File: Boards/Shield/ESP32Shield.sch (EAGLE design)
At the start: 30 parts, among them Q1 220mA/50V/3.5Ω, U1 5V

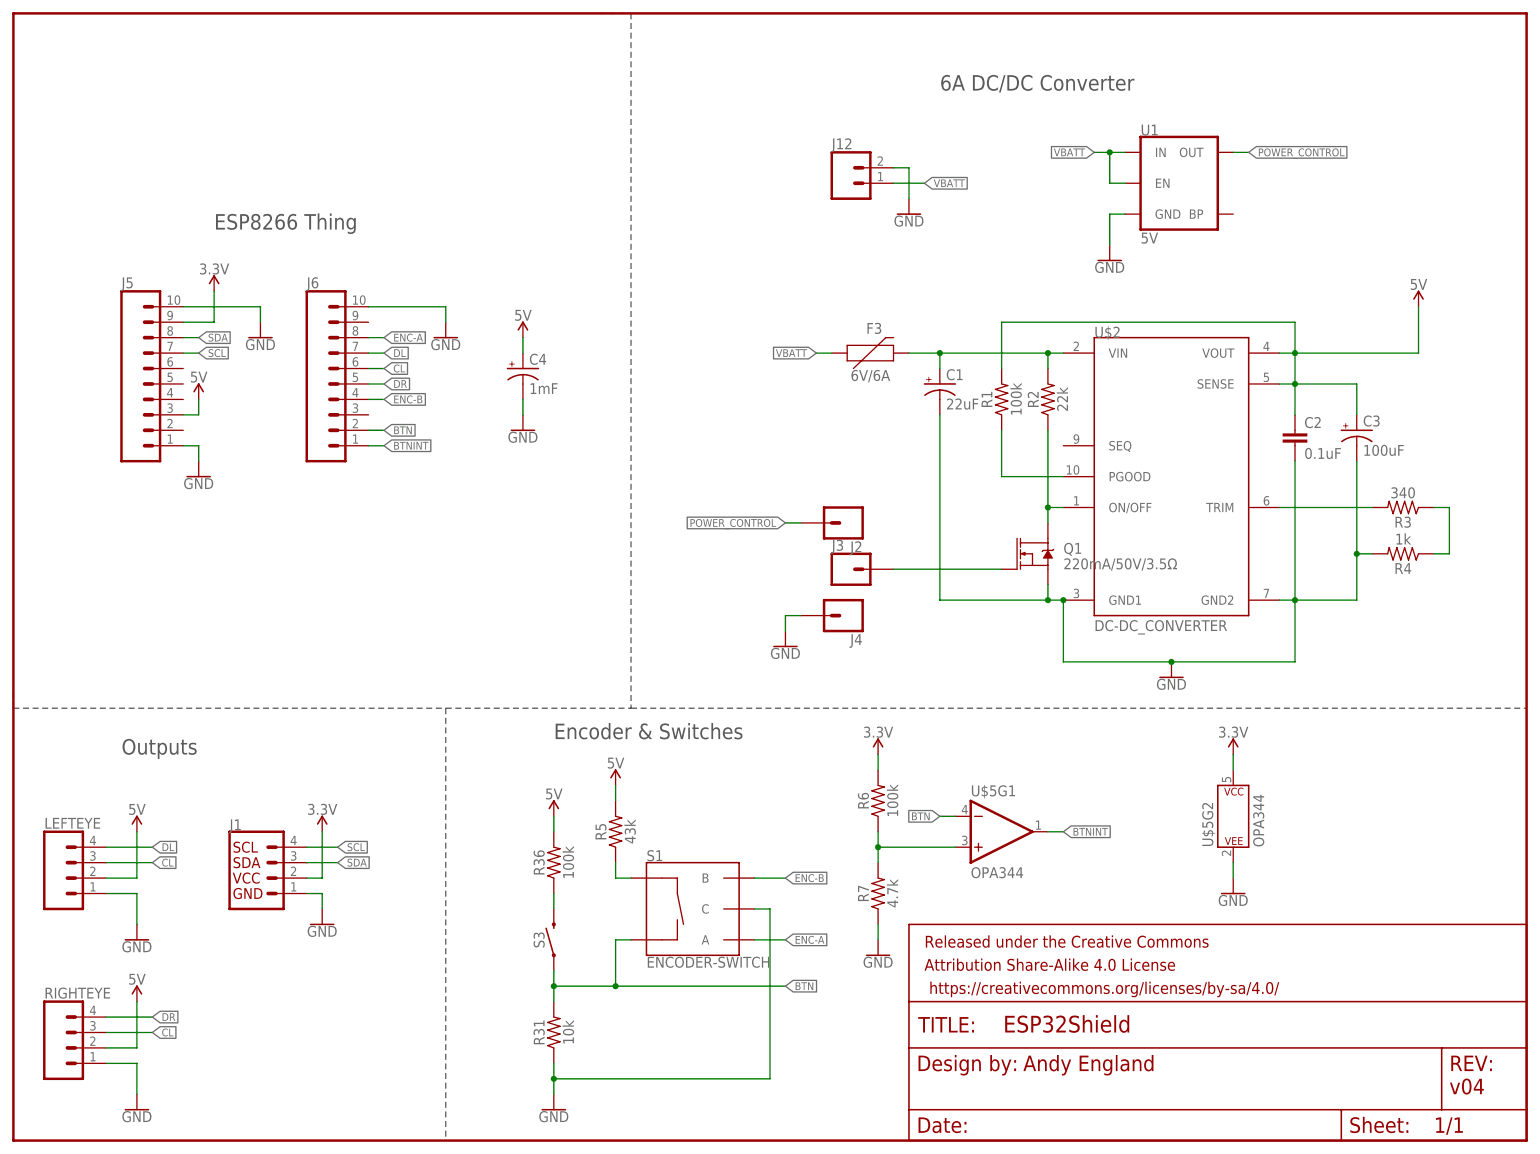
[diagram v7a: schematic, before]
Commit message: Updating to ESP32 WROOM
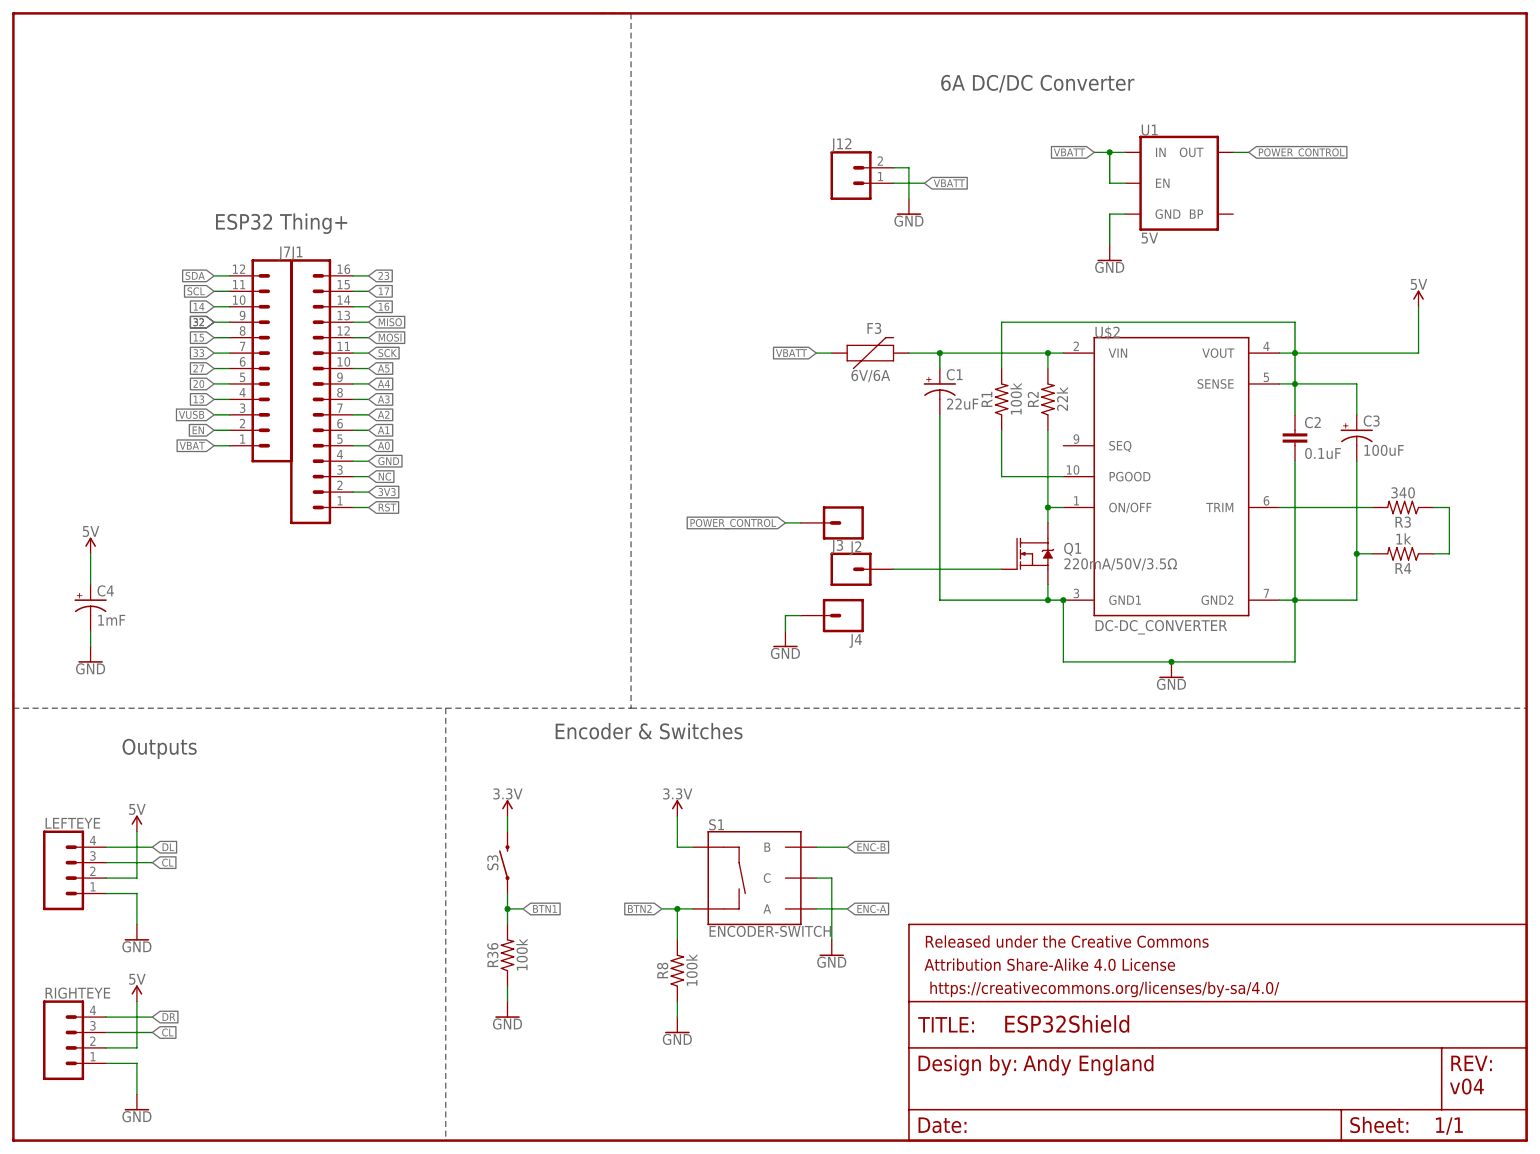
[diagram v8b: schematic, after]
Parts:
- removed J5, J6: (no value), SparkFun-Connectors:CONN_10NO_SILK_PTH_FEMALE
- removed R31: 10k, SparkFun-Resistors:10KOHM-0603-1/10W-1%
- removed R5: 43k, SparkFun-Resistors:43KOHM-0603-1/10W-1%
- removed R6: 100k, SparkFun-Resistors:100KOHM-0603-1/10W-1%
- removed R7: 4.7k, SparkFun-Resistors:4.7KOHM-0603-1/10W-1%
- removed U$5: OPA344, SparkFun-IC-Amplifiers:OPA344
- added J7: (no value), SparkFun-Connectors:CONN_12
- added R8: 100k, SparkFun-Resistors:100KOHM-0603-1/10W-1%
- J1: device SparkFun-Connectors:QWIIC_CONNECTORJS-1MM -> SparkFun-Connectors:CONN_16
- S3: value MOMENTARY-SWITCH-SPST-SMD-4.6X2.8MM -> MOMENTARY-SWITCH-SPST-SMD-5.2-REDUNDANT; device SparkFun-Switches:MOMENTARY-SWITCH-SPST-SMD-4.6X2.8MM -> SparkFun-Switches:MOMENTARY-SWITCH-SPST-SMD-5.2-REDUNDANT
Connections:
- removed net BTN: J6.2, R31.2, S1.SW-, S3.1, U$5G1.-IN
- removed net BTNINT: J6.1, U$5G1.OUT
- removed net N$17: R36.1, S3.2
- removed net N$6: R5.1, S1.SW+
- removed net N$9: R6.1, R7.2, U$5G1.+IN
- new net 13: J7.4
- new net 14: J7.10
- new net 15: J7.8
- new net 16: J1.14
- new net 17: J1.15
- new net 20: J7.5
- new net 23: J1.16
- new net 27: J7.6
- new net 32: J7.9
- new net 33: J7.7
- new net 3V3: J1.2
- new net A0: J1.5
- new net A1: J1.6
- new net A2: J1.7
- new net A3: J1.8
- new net A4: J1.9
- new net A5: J1.10
- new net BTN1: R36.2, S3.1
- new net BTN2: R8.2, S1.SW-
- new net EN: J7.2
- new net MISO: J1.13
- new net MOSI: J1.12
- new net NC: J1.3
- new net RST: J1.1
- new net SCK: J1.11
- new net VBAT: J7.1
- new net VUSB: J7.3
- net 3.3V: now also S1.SW+, S3.2; no longer J1.2, J5.9, R6.2, U$5G2.P$V+
- net 5V: no longer J5.3, R36.2, R5.2
- net CL: no longer J6.6
- net DL: no longer J6.7
- net DR: no longer J6.5
- net ENC-A: no longer J6.8
- net ENC-B: no longer J6.4
- net GND: now also J1.4, R36.1, R8.1; no longer J1.1, J5.1, J5.10, J6.10, R31.1, R7.1, U$5G2.P$V-
- net SCL: now also J7.11; no longer J1.4, J5.7
- net SDA: now also J7.12; no longer J1.3, J5.8
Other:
- note added: "ESP32 Thing+"
- note removed: "ESP8266 Thing"
- moved on the sheet: C4, R36, S1, S3
